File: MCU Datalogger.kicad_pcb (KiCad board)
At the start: 2 copper layers, 48.1 x 33.1 mm, 30 parts, among them J1 Conn_01x04_Pin, J2 Conn_01x04_Pin, J3 Conn_01x09_Pin, J4 Conn_02x03_Odd_Even, U1 24LC1025, U2 DS1337S_, U3 24LC1025, U4 ATMEGA328P-AU, Y1 32.768 KHZ, Y2 16 MHZ

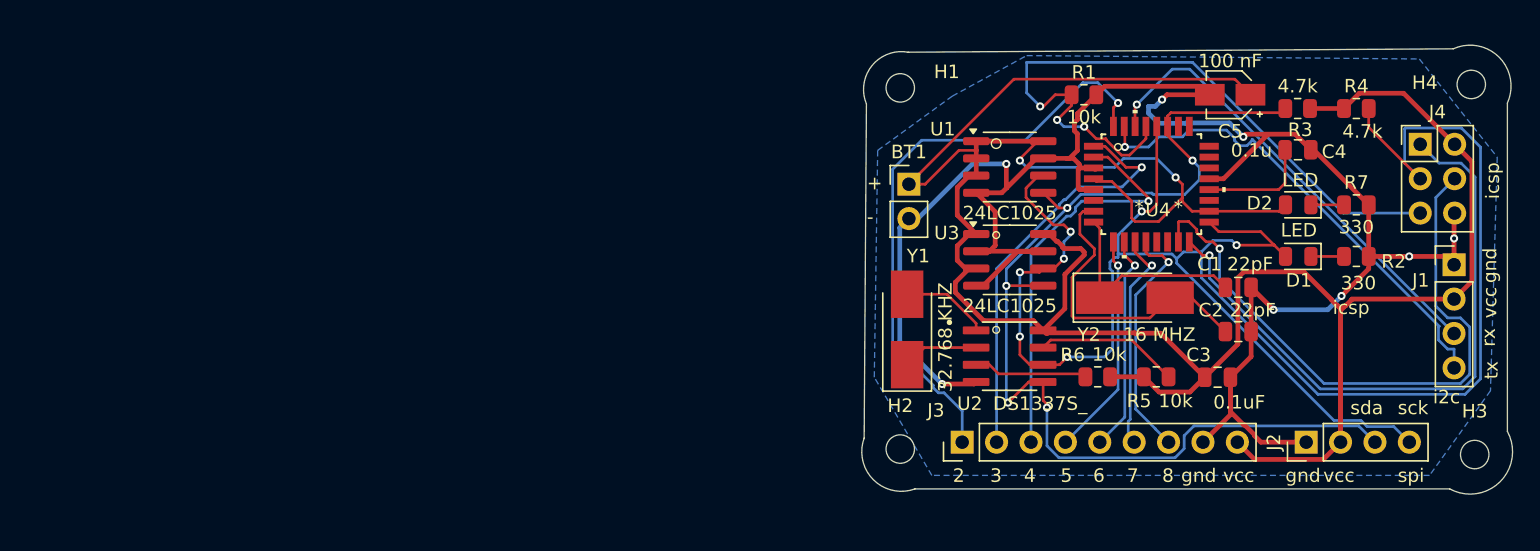
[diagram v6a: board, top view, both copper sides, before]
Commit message: completed full pcb 2 layer MCU datalogger
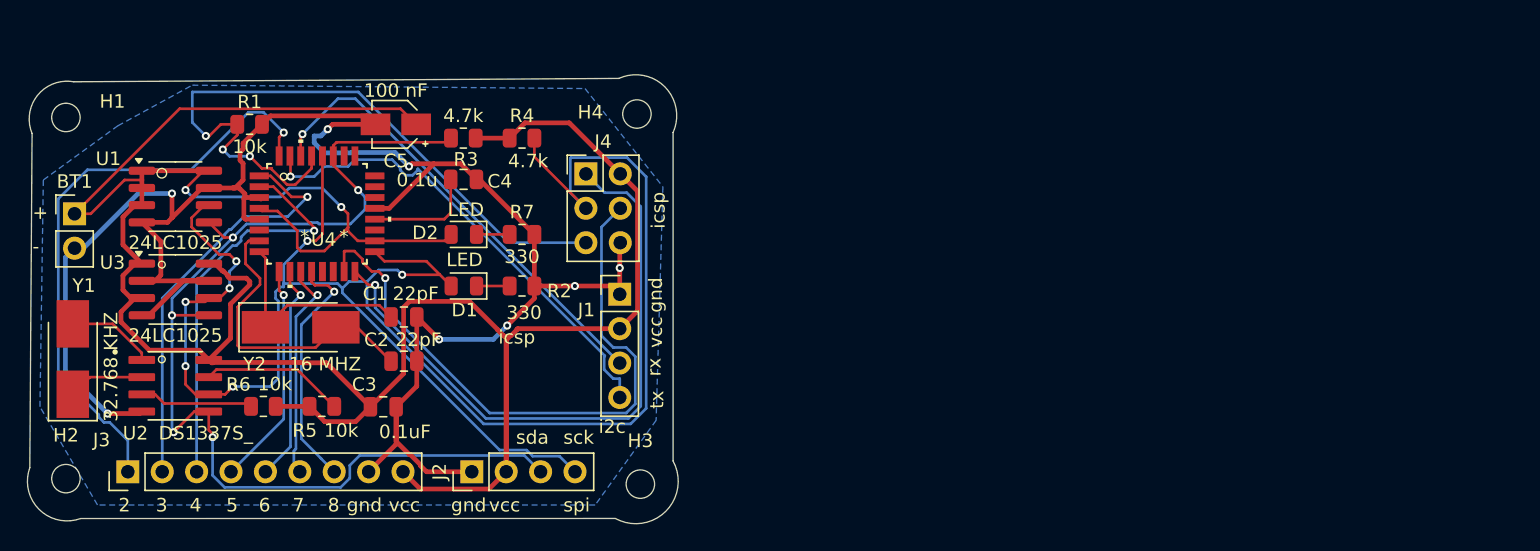
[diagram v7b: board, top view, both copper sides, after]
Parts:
- moved BT1 61.6 mm to (76.7, 97.2)
- moved C1 61.6 mm to (101.0, 104.8)
- moved C2 61.6 mm to (101.0, 108.1)
- moved D1 61.6 mm to (105.4, 102.5)
- moved D2 61.6 mm to (105.4, 98.7)
- moved H1 61.6 mm to (76.1, 90.1)
- moved H2 61.6 mm to (76.1, 116.7)
- moved H3 61.6 mm to (118.5, 117.1)
- moved J1 61.6 mm to (117.0, 103.1)
- moved J3 61.6 mm to (80.6, 116.2)
- moved R6 61.6 mm to (90.6, 111.4)
- moved U4 61.6 mm to (94.6, 97.2)
- moved C3 61.6 mm to (99.5, 111.4)
- moved C4 61.6 mm to (105.4, 94.6)
- moved C5 61.6 mm to (100.4, 90.6)
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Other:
- board text added: "0.2000 mm / 0.0000 mm"
- board text added: "0.3000 mm"
- board text added: "1.6000 mm"
- board text added: "48.0599 mm x 33.1575 mm"
- board text added: "BOARD CHARACTERISTICS"
- board text added: "Board Thickness:"
- board text added: "Board overall dimensions:"
- board text added: "Castellated pads:"
- board text added: "Copper Finish:"
- board text added: "Copper Layer Count:"
- board text added: "Edge card connectors:"
- board text added: "Impedance Control:"
- board text added: "Min hole diameter:"
- board text added: "Min track/spacing:"
- board text added: "No"
- board text added: "None"
- board text added: "Plated Board Edge:"

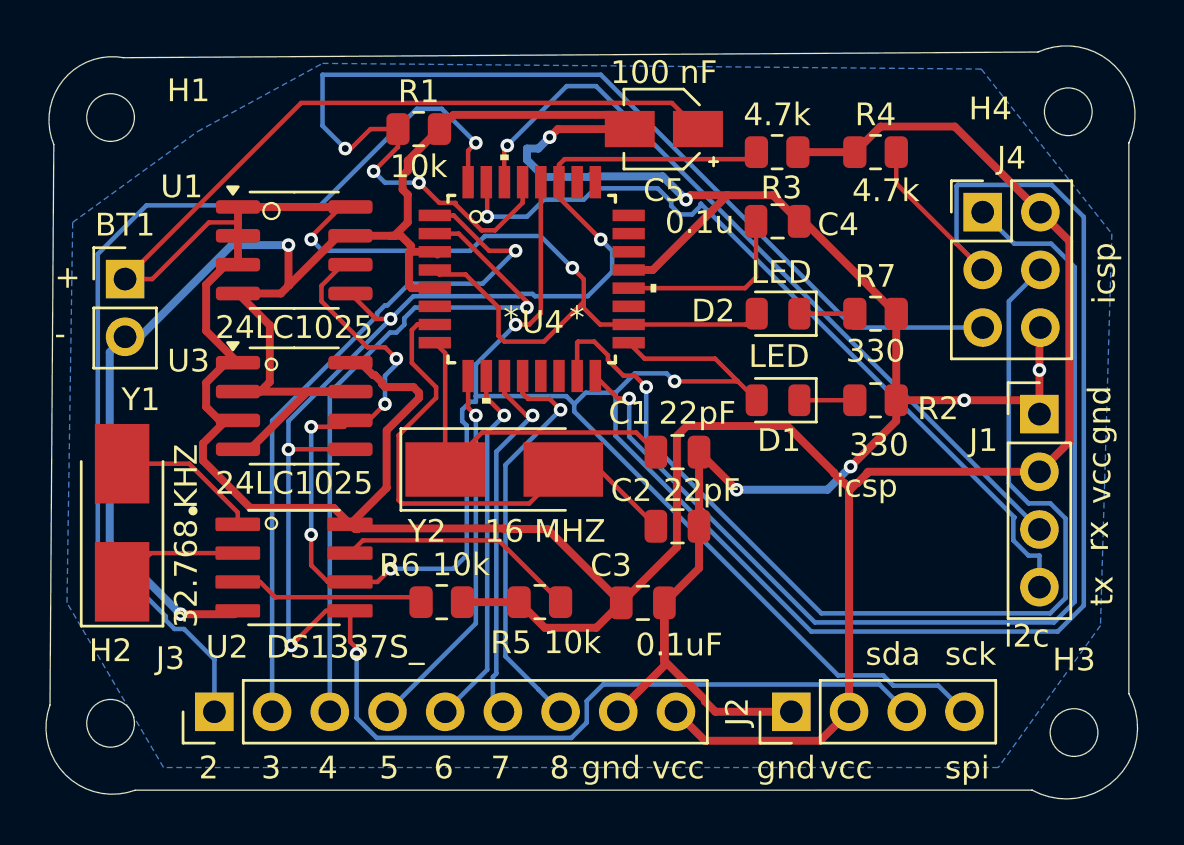
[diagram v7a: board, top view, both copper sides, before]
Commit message: completed full pcb 4 layer MCU datalogger
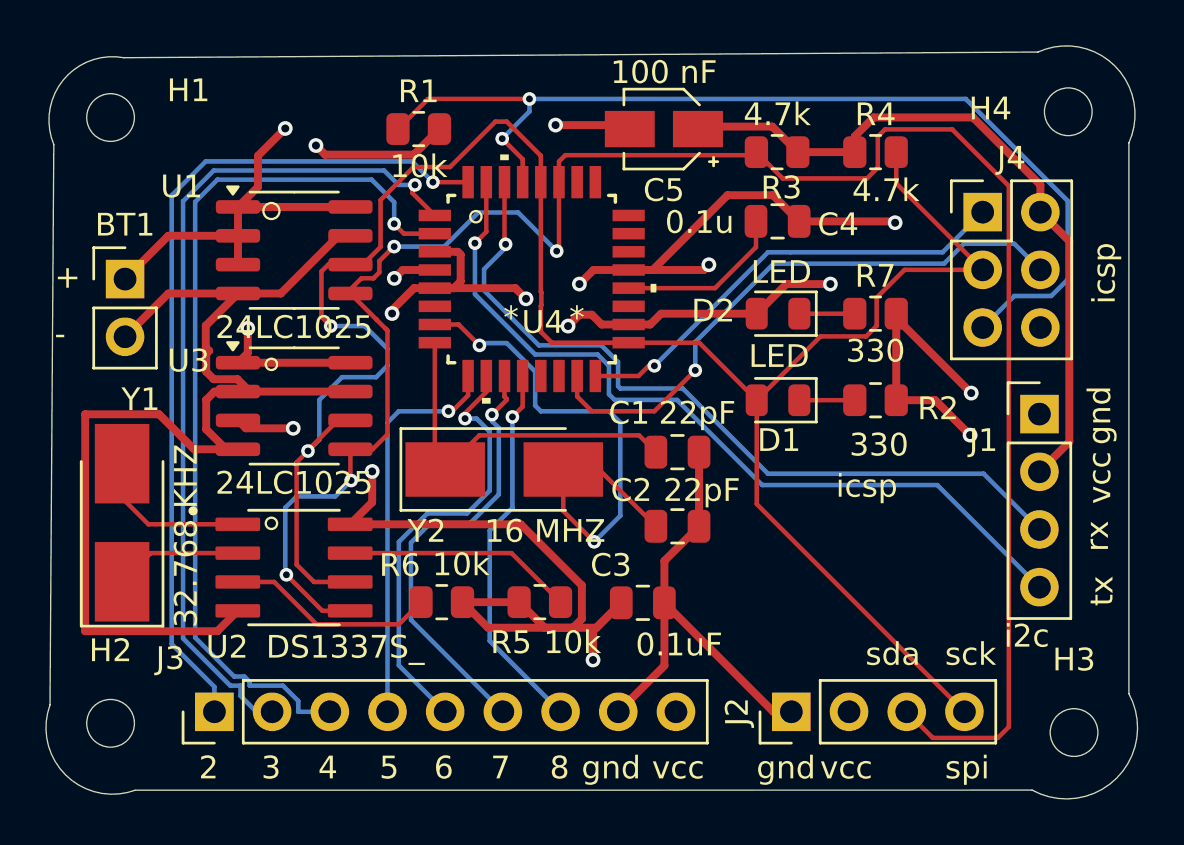
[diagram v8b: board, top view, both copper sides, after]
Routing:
- net GND: track 149.9 -> 210.9 mm, vias 8 -> 9
- net /SCK: track 147.6 -> 93.1 mm, vias 7 -> 2
- net /MISO: track 46.7 -> 20.0 mm
- net /MOSI: track 46.3 -> 25.8 mm
- net /D4: track 30.0 -> 39.3 mm
- net /D3: track 30.9 -> 38.3 mm
- net /RESET: track 51.4 -> 44.5 mm, vias 3 -> 2
- net /D2: track 44.3 -> 37.6 mm
- net /SDA: track 81.6 -> 87.8 mm, vias 5 -> 4
- net /D6: track 16.2 -> 19.4 mm
- net /D7: track 16.4 -> 19.5 mm
- net Net-(U4-PB6(PCINT6/XTAL1/TOSC1)): track 22.8 -> 25.5 mm, vias 0 -> 2
- net /D8: track 18.0 -> 16.7 mm
- net /D5: track 16.5 -> 17.6 mm
- net Net-(U2-~{INTA}): track 8.44 -> 9.25 mm
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- added copper zone on In2.Cu, net /vcc
- added copper zone on In1.Cu, net GND
- removed copper zone on B.Cu, net GND
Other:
- copper layers 2 -> 4
